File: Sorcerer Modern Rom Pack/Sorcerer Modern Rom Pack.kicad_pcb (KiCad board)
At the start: 2 copper layers, 119.4 x 73.3 mm, 88 parts, among them J1 ROMRD15, J10 A11, J11 A13, J12 A12, J13 A, J14 A, J15 A, J16 A, J17 A, J18 C, J19 B, J2 A14, J20 A, J21 A, J22 A, J23 A, J24 A, J25 A, J26 A, J27 A, J28 Sorcerer Cart Slot, J29 0 ENABLE, J3 ROMRD15, J30 1 ENABLE, J31 4 ENABLE, J32 5 ENABLE, J33 1 PROM, J34 2 PROM, J35 A, J36 A, J37 A, J38 A, J39 A, J4 A12, J40 A, J41 A, J42 A, J43 A, J44 A, J45 A, J46 A, J47 A, J48 A, J49 A, J5 Conn_01x01, J50 A, J51 A, J52 A, J53 A, J54 A, J55 A, J56 A, J57 A, J58 A, J59 A, J6 Conn_01x01, J60 A, J61 A, J62 A, J63 A, J64 A, J65 A, J66 A, J67 A, J68 A, J69 RAM cut, J7 A, J8 A14, J9 A10, U1 2716, U2 2716, U3 2716, U4 2716, U5 74LS11, U6 74LS138

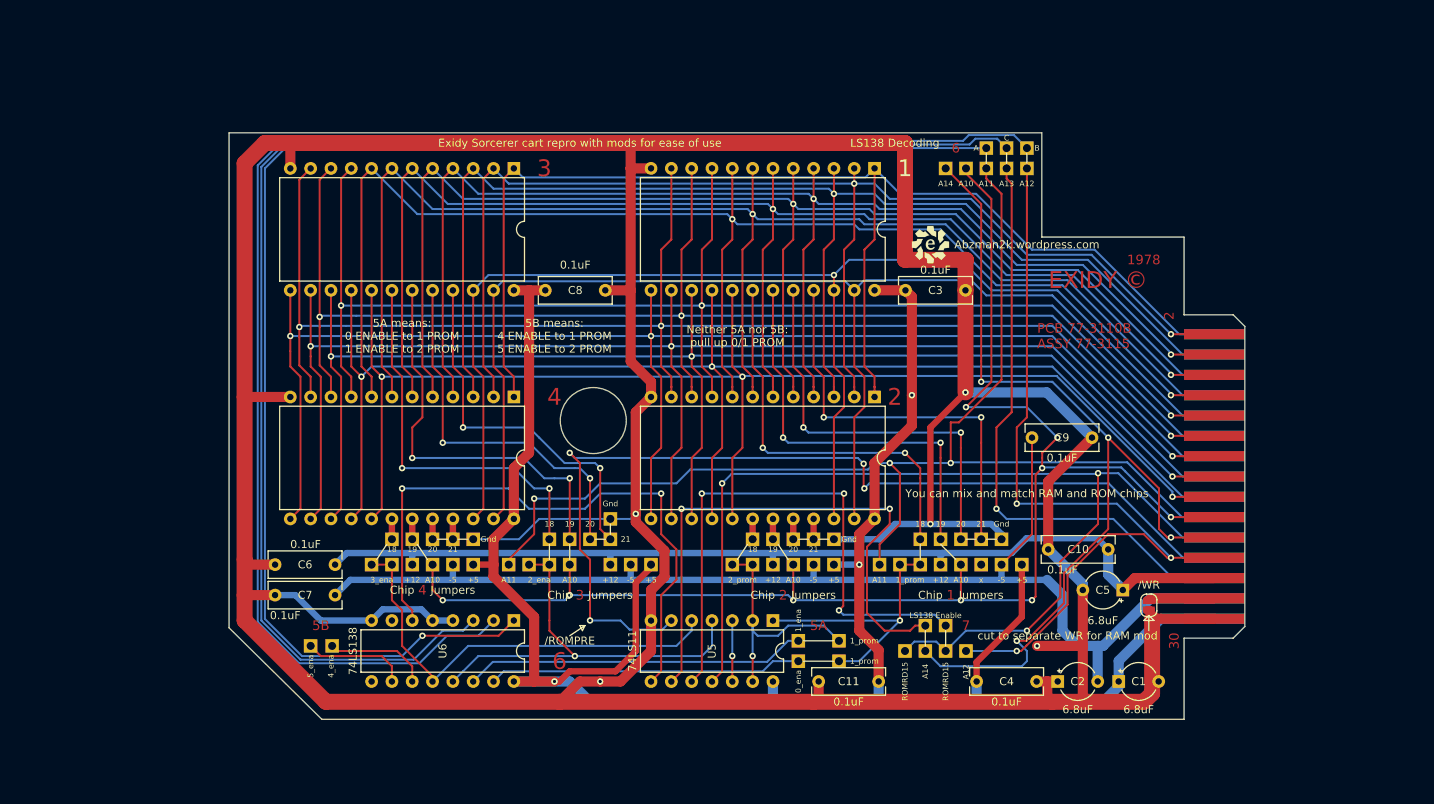
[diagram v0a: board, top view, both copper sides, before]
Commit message: silk for bank switched ROM PCB
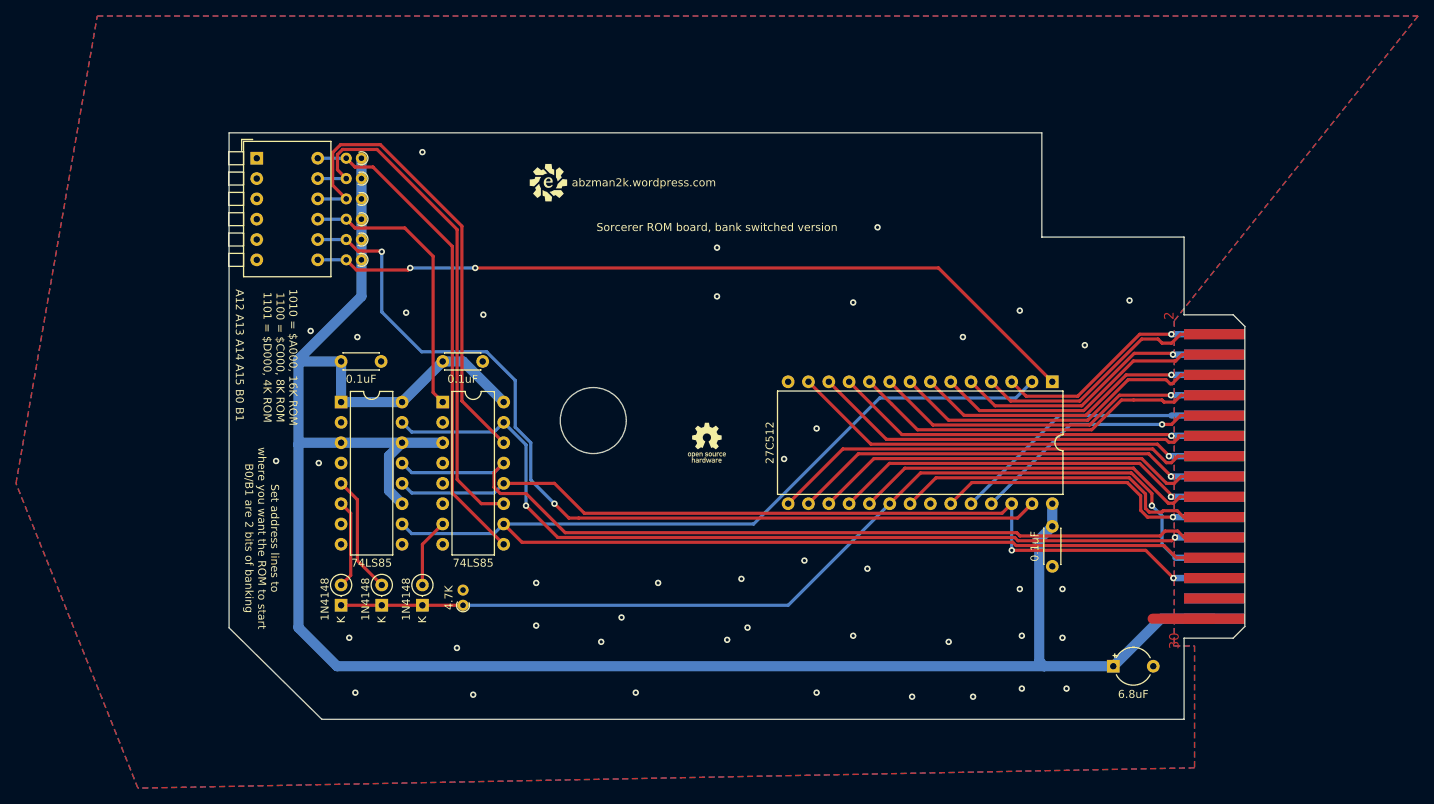
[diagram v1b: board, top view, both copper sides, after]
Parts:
- removed C10, C11, C6, C7, C9: 0.1uF, Capacitor_THT:C_Rect_L9.0mm_W3.2mm_P7.50mm_MKT
- removed C2, C5: 6.8uF, Capacitor_THT:CP_Radial_Tantal_D4.5mm_P5.00mm
- removed J1, J3: ROMRD15, Evan's misc parts:PinHeader_1x01_P2.54mm_Vertical_nosilk
- removed J10: A11, Evan's misc parts:PinHeader_1x01_P2.54mm_Vertical_nosilk
- removed J11: A13, Evan's misc parts:PinHeader_1x01_P2.54mm_Vertical_nosilk
- removed J12, J4: A12, Evan's misc parts:PinHeader_1x01_P2.54mm_Vertical_nosilk
- removed J13, J14, J15, J16, J17, J20, J21, J22, J23, J24, J25, J26, J27, J35, J36, J37, J38, J39, J40, J41, J42, J43, J44, J45, J46, J47, J48, J49, J50, J51, J52, J53, J54, J55, J56, J57, J58, J59, J60, J61, J62, J63, J64, J65, J66, J67, J68, J7: A, Evan's misc parts:PinHeader_1x01_P2.54mm_Vertical_nosilk
- removed J18: C, Evan's misc parts:PinHeader_1x01_P2.54mm_Vertical_nosilk
- removed J19: B, Evan's misc parts:PinHeader_1x01_P2.54mm_Vertical_nosilk
- removed J2, J8: A14, Evan's misc parts:PinHeader_1x01_P2.54mm_Vertical_nosilk
- removed J29: 0 ENABLE, Evan's misc parts:PinHeader_1x01_P2.54mm_Vertical_nosilk
- removed J30: 1 ENABLE, Evan's misc parts:PinHeader_1x01_P2.54mm_Vertical_nosilk
- removed J31: 4 ENABLE, Evan's misc parts:PinHeader_1x01_P2.54mm_Vertical_nosilk
- removed J32: 5 ENABLE, Evan's misc parts:PinHeader_1x01_P2.54mm_Vertical_nosilk
- removed J33: 1 PROM, Evan's misc parts:PinHeader_1x01_P2.54mm_Vertical_nosilk
- removed J34: 2 PROM, Evan's misc parts:PinHeader_1x01_P2.54mm_Vertical_nosilk
- removed J5, J6: Conn_01x01, Evan's misc parts:PinHeader_1x01_P2.54mm_Vertical_nosilk
- removed J69: RAM cut, Jumper:SolderJumper-2_P1.3mm_Open_RoundedPad1.0x1.5mm
- removed J9: A10, Evan's misc parts:PinHeader_1x01_P2.54mm_Vertical_nosilk
- removed U4: 2716, Package_DIP:DIP-24_W15.24mm
- removed U5: 74LS11, Package_DIP:DIP-14_W7.62mm
- removed U6: 74LS138, Package_DIP:DIP-16_W7.62mm
- added D1: 1N4148, Diode_THT:D_DO-35_SOD27_P2.54mm_Vertical_KathodeUp, F.Cu at (88.9, 129.5)
- added D2: 1N4148, Diode_THT:D_DO-35_SOD27_P2.54mm_Vertical_KathodeUp, F.Cu at (83.8, 129.5)
- added D3: 1N4148, Diode_THT:D_DO-35_SOD27_P2.54mm_Vertical_KathodeUp, F.Cu at (94.0, 129.5)
- added R1: 4.7K, Resistor_THT:R_Axial_DIN0204_L3.6mm_D1.6mm_P1.90mm_Vertical, F.Cu at (86.4, 73.7)
- added R2: 4.7K, Resistor_THT:R_Axial_DIN0204_L3.6mm_D1.6mm_P1.90mm_Vertical, F.Cu at (86.4, 76.2)
- added R3: 4.7K, Resistor_THT:R_Axial_DIN0204_L3.6mm_D1.6mm_P1.90mm_Vertical, F.Cu at (86.4, 78.7)
- added R4: 4.7K, Resistor_THT:R_Axial_DIN0204_L3.6mm_D1.6mm_P1.90mm_Vertical, F.Cu at (86.4, 81.3)
- added R5: 4.7K, Resistor_THT:R_Axial_DIN0204_L3.6mm_D1.6mm_P1.90mm_Vertical, F.Cu at (86.4, 83.8)
- added R6: 4.7K, Resistor_THT:R_Axial_DIN0204_L3.6mm_D1.6mm_P1.90mm_Vertical, F.Cu at (86.4, 86.4)
- added R7: 4.7K, Resistor_THT:R_Axial_DIN0204_L3.6mm_D1.6mm_P1.90mm_Vertical, F.Cu at (99.1, 129.5)
- added SW1: SW_DIP_x06, Button_Switch_THT:SW_DIP_SPSTx06_Piano_10.8x16.8mm_W7.62mm_P2.54mm, F.Cu at (73.3, 73.7)
- C3, C4, C8: footprint Capacitor_THT:C_Rect_L9.0mm_W3.2mm_P7.50mm_MKT -> Capacitor_THT:C_Disc_D4.3mm_W1.9mm_P5.00mm
- G***: moved to F.Cu
- U1, U2: value 2716 -> 74LS85; footprint Package_DIP:DIP-24_W15.24mm -> Package_DIP:DIP-16_W7.62mm
- U3: value 2716 -> 27C512; footprint Package_DIP:DIP-24_W15.24mm -> Package_DIP:DIP-28_W15.24mm
- moved C4 88.9 mm to (83.8, 99.1)
- moved U3 72.4 mm to (172.7, 101.6)
- moved U2 66.7 mm to (83.8, 104.1), turned to 0 degrees
- moved U1 61.4 mm to (96.5, 104.1), turned to 0 degrees
- moved G*** 48.4 mm to (109.7, 76.7)
- moved G*** 41.5 mm to (129.5, 109.2), turned to 0 degrees
- moved C3 34.7 mm to (172.7, 119.7), turned to -90 degrees
- moved C8 15.6 mm to (96.5, 99.1)
- moved C1 2.02 mm to (180.3, 137.2)
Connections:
- U1 pad 1: 1 -> Net-(R4-Pad2)
- U1 pad 10: 12 -> 24
- U1 pad 11: 13 -> Net-(R2-Pad2)
- U1 pad 12: 30 -> 25
- U1 pad 13: 14 -> 22
- U1 pad 14: 15 -> Net-(R3-Pad2)
- U1 pad 15: 16 -> 21
- U1 pad 16: 17 -> 29
- U1 pad 2: 2 -> unconnected-(U1-Pad2)
- U1 pad 3: 3 -> 29
- U1 pad 4: 4 -> unconnected-(U1-Pad4)
- U1 pad 5: 5 -> unconnected-(U1-Pad5)
- U1 pad 6: 6 -> unconnected-(U1-Pad6)
- U1 pad 7: 7 -> Net-(D3-Pad2)
- U1 pad 8: 8 -> 30
- U1 pad 9: 11 -> Net-(R1-Pad2)
- U2 pad 1: 1 -> 29
- U2 pad 10: 12 -> 24
- U2 pad 11: 13 -> 29
- U2 pad 12: 30 -> 25
- U2 pad 13: 14 -> 22
- U2 pad 14: 15 -> 29
- U2 pad 15: 16 -> 21
- U2 pad 16: 17 -> 29
- U2 pad 2: 2 -> unconnected-(U2-Pad2)
- U2 pad 3: 3 -> 29
- U2 pad 4: 4 -> unconnected-(U2-Pad4)
- U2 pad 5: 5 -> Net-(D1-Pad2)
- U2 pad 6: 6 -> Net-(D2-Pad2)
- U2 pad 7: 7 -> unconnected-(U2-Pad7)
- U2 pad 8: 8 -> 30
- U2 pad 9: 11 -> 30
- U3 pad 1: 1 -> ROM15
- U3 pad 10: 12 -> 8
- U3 pad 11: 13 -> 11
- U3 pad 12: 30 -> 12
- U3 pad 13: 14 -> 13
- U3 pad 14: 15 -> 30
- U3 pad 15: 16 -> 14
- U3 pad 16: 17 -> 15
- U3 pad 17: 18 -> 16
- U3 pad 18: Net-(J55-Pad1) -> 17
- U3 pad 19: Net-(J53-Pad1) -> 18
- U3 pad 2: 2 -> 24
- U3 pad 20: Net-(J51-Pad1) -> 23
- U3 pad 21: Net-(J49-Pad1) -> 20
- U3 pad 22: 9 -> 30
- U3 pad 23: 10 -> 19
- U3 pad 24: 29 -> 9
- U3 pad 3: 3 -> 1
- U3 pad 4: 4 -> 2
- U3 pad 5: 5 -> 3
- U3 pad 6: 6 -> 4
- U3 pad 7: 7 -> 5
- U3 pad 8: 8 -> 6
- U3 pad 9: 11 -> 7
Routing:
- net 30: track 576.6 -> 7.72 mm, vias 5 -> 43
- net Net-(J19-Pad1): track 189.3 -> 0.00 mm
- net Net-(J17-Pad1): track 182.4 -> 0.00 mm, vias 1 -> 0
- net Net-(J18-Pad1): track 182.3 -> 0.00 mm
- net 27: track 148.7 -> 0.00 mm
- net 20: track 183.1 -> 42.6 mm, vias 9 -> 0
- net 7: track 173.8 -> 44.4 mm
- net 8: track 176.5 -> 47.6 mm, vias 2 -> 0
- net 9: track 163.4 -> 35.0 mm, vias 1 -> 0
- net 5: track 167.7 -> 39.3 mm
- net 6: track 170.3 -> 42.8 mm, vias 2 -> 0
- net 3: track 161.5 -> 34.5 mm
- net 1: track 156.3 -> 29.3 mm, vias 0 -> 1
- net 4: track 164.2 -> 37.4 mm, vias 2 -> 0
- net 11: track 175.2 -> 48.5 mm, vias 2 -> 1
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- added copper zone on B.Cu, net 30
- added copper zone on F.Cu, net 30
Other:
- board text added: "1010 = $A000, 16K ROM 1100 = $C000, 8K ROM 1101 = $D000, 4K ROM"
- board text added: "A12 A13 A14 A15 B0 B1"
- board text added: "Set address lines to where you want the ROM to start B0/B1 are 2 bits of banking"
- board text added: "Sorcerer ROM board, bank switched version"
- board text added: "abzman2k.wordpress.com"
- board text removed: "+12"
- board text removed: "+5"
- board text removed: "-5"
- board text removed: "/ROMPRE"
- board text removed: "/WR"
- board text removed: "0_ena"
- board text removed: "1"
- board text removed: "16K ROM PAC, 4K ROMS 5B 6 - A to A12, B to A13, C to A14 7 - ROMRD15 and ROMRD15 A000-AFFF - ROM 3 B000-BFFF - ROM 4 C000-CFFF - ROM 1 D000-DFFF - ROM 2"
- board text removed: "18"
- board text removed: "19"
- board text removed: "1978"
- board text removed: "1_ena"
- board text removed: "1_prom"
- board text removed: "20"
- board text removed: "21"
- board text removed: "2708: 18 - Gnd 19 - +12 20 - /CS 21 - -5"
- board text removed: "2716: 18 - Gnd 19 - A10 20 - /CS 21 - +5"
- board text removed: "2732: 18 - Gnd 19 - A10 20 - /CS 21 - A11"
- board text removed: "2_ena"
- board text removed: "2_prom"
- board text removed: "3"
- board text removed: "3_ena"
- board text removed: "4"
- board text removed: "4K ROM PAC, 1K ROMS 5A 6 - A to A10, B to A11, C to A13 7 - A12 and A14 D000-D3FF - ROM 1 D400-D7FF - ROM 2 D800-DBFF - ROM 3 DC00-DFFF - ROM 4"
- board text removed: "4K ROM PAC, 2K ROMS 5A 6 - A to A12, B to A11, C to A13 7 - A12 and A14 D000-D7FF - ROM 2 D800-DFFF - ROM 4"
- board text removed: "4K ROM PAC, 2K ROMS 6 - A to A11, B to A12, C to A13 7 - ROMRD15 and A14 D000-D7FF - ROM 3 D800-DFFF - ROM 4"
- board text removed: "4K ROM PAC, 4K ROM 6 - A to A13, B to A12, C to A13 7 - ROMRD15 and A14 D000-DFFF - ROM 3"
- board text removed: "4_ena"
- board text removed: "5A"
- board text removed: "5A means: 0 ENABLE to 1 PROM 1 ENABLE to 2 PROM"
- board text removed: "5B"
- board text removed: "5B means: 4 ENABLE to 1 PROM 5 ENABLE to 2 PROM"
- board text removed: "5_ena"
- board text removed: "6"
- board text removed: "6116: 18 - /CS 19 - A10 20 - Gnd 21 - /WE"
- board text removed: "7"
- board text removed: "8K ROM PAC, 2K ROMS 5A 6 - A to A11, B to A12, C to A13 7 - ROMRD15 and A14 C000-C7FF - ROM 1 C800-CFFF - ROM 2 D000-D7FF - ROM 3 D800-DFFF - ROM 4"
- board text removed: "8K ROM PAC, 4K ROMS 5A 6 - A to A13, B to A12, C to A13 7 - ROMRD15 and A14 C000-CFFF - ROM 1 D000-DFFF - ROM 3"
- board text removed: "A"
- board text removed: "A10"
- board text removed: "A11"
- board text removed: "A12"
- board text removed: "A13"
- board text removed: "A14"
- board text removed: "AM9218/factory PROM: 18 - /CS 19 - A10 20 - Gnd 21 - Gnd"
- board text removed: "Abzman2k.wordpress.com"
- board text removed: "B"
- board text removed: "C"
- board text removed: "Chip"
- board text removed: "EXIDY ©"
- board text removed: "Exidy Sorcerer cart repro with mods for ease of use"
- board text removed: "Gnd"
- board text removed: "Jumpers"
- board text removed: "LS138 Decoding"
- board text removed: "LS138 Enable"
- board text removed: "Neither 5A nor 5B: pull up 0/1 PROM"
- board text removed: "PCB 77-3110B ASSY 77-3115"
- board text removed: "ROMRD15"
- board text removed: "TMS2716: 18 - /CS 19 - +12 20 - A10 21 - -5"
- board text removed: "You can mix and match RAM and ROM chips"
- board text removed: "cut to separate WR for RAM mod"
- board text removed: "if not using +12v, omit C5, C6 and C10"
- board text removed: "if not using -5v, omit C2, C7 and C9"
- board text removed: "x"
